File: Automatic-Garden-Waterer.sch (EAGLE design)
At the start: 14 parts, among them K1 AQG12105, X1 6ESRM-P

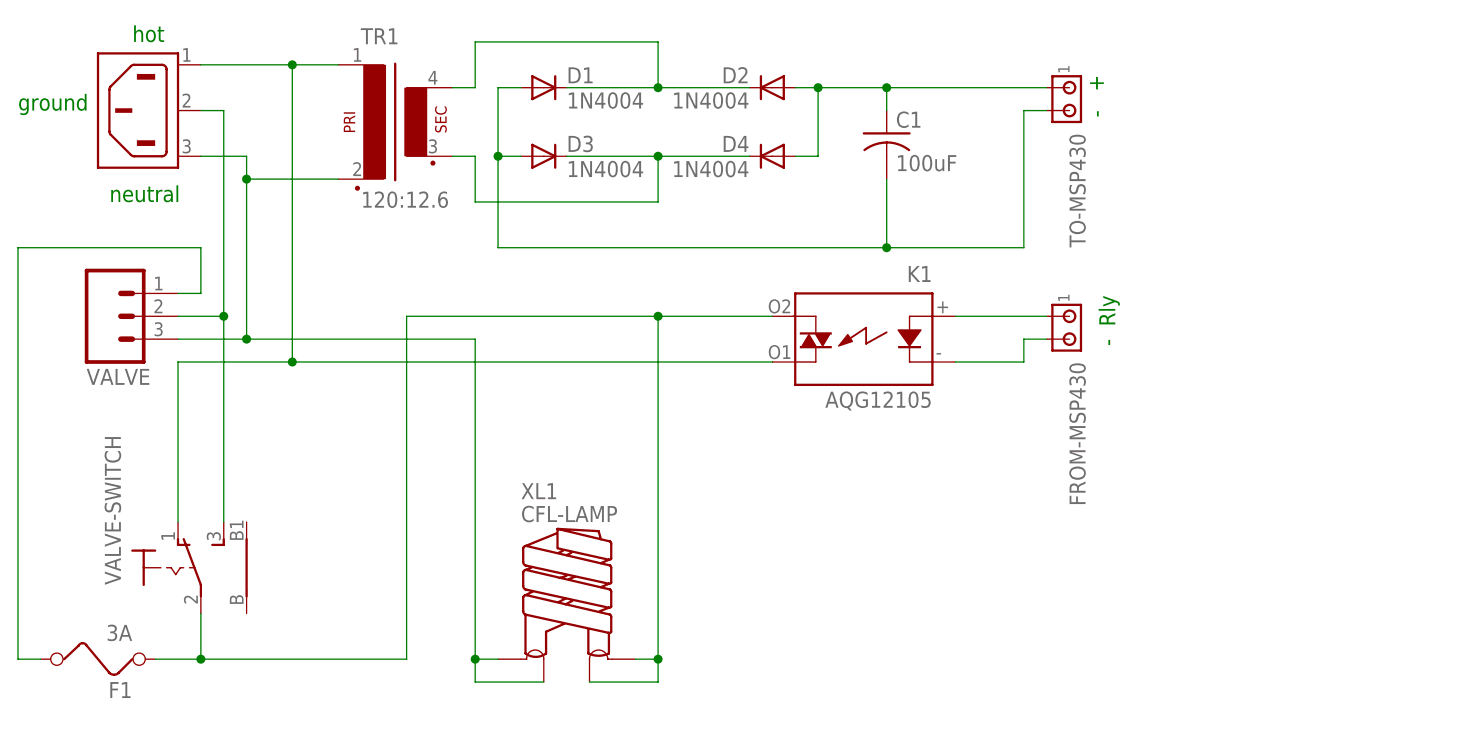
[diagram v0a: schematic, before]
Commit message: modified because valve is normally open
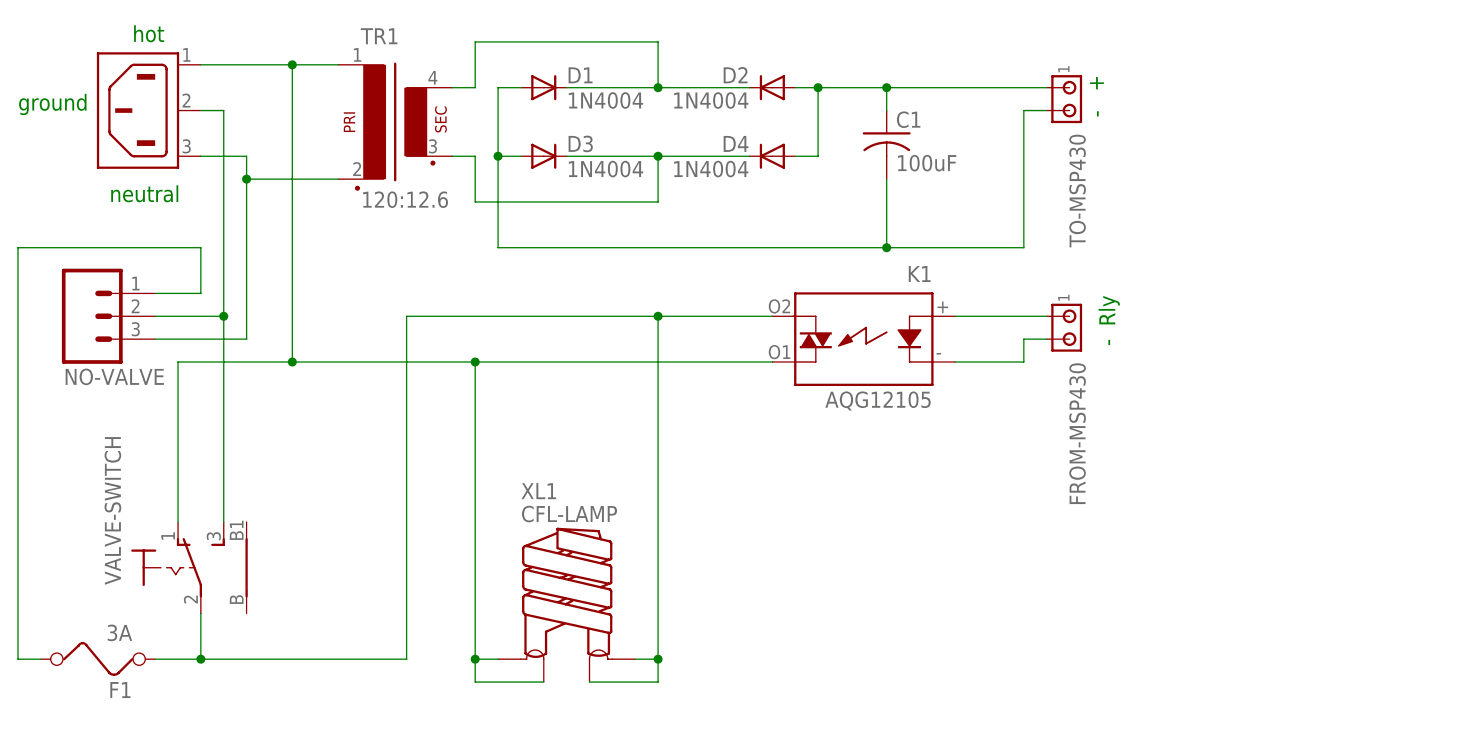
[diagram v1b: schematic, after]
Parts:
- removed VALVE: (no value), SparkFun:M03PTH
- added NO-VALVE: (no value), SparkFun:M03PTH
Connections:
- removed net N$5: K1.DS2, TR1.P1, VALVE-SWITCH.O, X1.AC1
- new net N$2: NO-VALVE.3, TR1.P2, X1.AC2
- net N$10: now also NO-VALVE.2; no longer VALVE.2
- net N$13: now also NO-VALVE.1; no longer VALVE.1
- net N$6: now also K1.DS2, TR1.P1, VALVE-SWITCH.O, X1.AC1; no longer TR1.P2, VALVE.3, X1.AC2
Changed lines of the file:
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@@
 <part name="X1" library="con-tycoelectronics" deviceset="6ESRM-P" device=""/>
 <part name="XL1" library="ir" deviceset="CFL-LAMP" device=""/>
-<part name="VALVE" library="SparkFun" deviceset="M03" device="PTH"/>
+<part name="NO-VALVE" library="SparkFun" deviceset="M03" device="PTH"/>
 <part name="VALVE-SWITCH" library="switch" deviceset="316-917" device=""/>
 </parts>
@@
 <instance part="X1" gate="G$1" x="-15.24" y="53.34" rot="MR0"/>
 <instance part="XL1" gate="G$1" x="27.94" y="-2.54"/>
-<instance part="VALVE" gate="G$1" x="-22.86" y="30.48" rot="MR180"/>
+<instance part="NO-VALVE" gate="G$1" x="-25.4" y="30.48" rot="MR180"/>
 <instance part="VALVE-SWITCH" gate="1" x="-15.24" y="2.54"/>
 </instances>
@@
 <net name="N$6" class="0">
 <segment>
-<pinref part="X1" gate="G$1" pin="AC2"/>
-<wire x1="-12.7" y1="48.26" x2="-7.62" y2="48.26" width="0.1524" layer="91"/>
-<wire x1="-7.62" y1="48.26" x2="-7.62" y2="45.72" width="0.1524" layer="91"/>
-<pinref part="TR1" gate="1" pin="P2"/>
-<wire x1="-7.62" y1="45.72" x2="2.54" y2="45.72" width="0.1524" layer="91"/>
-<pinref part="VALVE" gate="G$1" pin="3"/>
-<wire x1="-15.24" y1="27.94" x2="-7.62" y2="27.94" width="0.1524" layer="91"/>
-<wire x1="-7.62" y1="27.94" x2="-7.62" y2="45.72" width="0.1524" layer="91"/>
-<junction x="-7.62" y="45.72"/>
 <pinref part="XL1" gate="G$1" pin="1"/>
 <wire x1="20.32" y1="-7.62" x2="17.78" y2="-7.62" width="0.1524" layer="91"/>
@@
 <wire x1="17.78" y1="-10.16" x2="17.78" y2="-7.62" width="0.1524" layer="91"/>
 <junction x="17.78" y="-7.62"/>
-<wire x1="-7.62" y1="27.94" x2="17.78" y2="27.94" width="0.1524" layer="91"/>
-<wire x1="17.78" y1="27.94" x2="17.78" y2="-7.62" width="0.1524" layer="91"/>
-<junction x="-7.62" y="27.94"/>
-</segment>
-</net>
-<net name="N$5" class="0">
-<segment>
 <pinref part="TR1" gate="1" pin="P1"/>
 <pinref part="X1" gate="G$1" pin="AC1"/>
@@
 <wire x1="-2.54" y1="58.42" x2="-2.54" y2="25.4" width="0.1524" layer="91"/>
 <pinref part="K1" gate="A" pin="DS2"/>
-<wire x1="50.8" y1="25.4" x2="-2.54" y2="25.4" width="0.1524" layer="91"/>
+<wire x1="50.8" y1="25.4" x2="17.78" y2="25.4" width="0.1524" layer="91"/>
 <pinref part="VALVE-SWITCH" gate="1" pin="O"/>
+<wire x1="17.78" y1="25.4" x2="-2.54" y2="25.4" width="0.1524" layer="91"/>
 <wire x1="-15.24" y1="7.62" x2="-15.24" y2="25.4" width="0.1524" layer="91"/>
 <wire x1="-15.24" y1="25.4" x2="-2.54" y2="25.4" width="0.1524" layer="91"/>
 <junction x="-2.54" y="25.4"/>
+<wire x1="17.78" y1="-7.62" x2="17.78" y2="25.4" width="0.1524" layer="91"/>
+<junction x="17.78" y="25.4"/>
 </segment>
 </net>
@@
 <wire x1="-12.7" y1="53.34" x2="-10.16" y2="53.34" width="0.1524" layer="91"/>
 <wire x1="-10.16" y1="53.34" x2="-10.16" y2="30.48" width="0.1524" layer="91"/>
-<pinref part="VALVE" gate="G$1" pin="2"/>
-<wire x1="-10.16" y1="30.48" x2="-15.24" y2="30.48" width="0.1524" layer="91"/>
+<pinref part="NO-VALVE" gate="G$1" pin="2"/>
+<wire x1="-10.16" y1="30.48" x2="-17.78" y2="30.48" width="0.1524" layer="91"/>
 <junction x="-10.16" y="30.48"/>
 <pinref part="VALVE-SWITCH" gate="1" pin="S"/>
@@
 <wire x1="-33.02" y1="38.1" x2="-12.7" y2="38.1" width="0.1524" layer="91"/>
 <wire x1="-12.7" y1="38.1" x2="-12.7" y2="33.02" width="0.1524" layer="91"/>
-<pinref part="VALVE" gate="G$1" pin="1"/>
-<wire x1="-12.7" y1="33.02" x2="-15.24" y2="33.02" width="0.1524" layer="91"/>
+<pinref part="NO-VALVE" gate="G$1" pin="1"/>
+<wire x1="-12.7" y1="33.02" x2="-17.78" y2="33.02" width="0.1524" layer="91"/>
 </segment>
 </net>
+<net name="N$2" class="0">
+<segment>
+<pinref part="TR1" gate="1" pin="P2"/>
+<pinref part="X1" gate="G$1" pin="AC2"/>
+<wire x1="-12.7" y1="48.26" x2="-7.62" y2="48.26" width="0.1524" layer="91"/>
+<wire x1="-7.62" y1="48.26" x2="-7.62" y2="45.72" width="0.1524" layer="91"/>
+<wire x1="-7.62" y1="45.72" x2="2.54" y2="45.72" width="0.1524" layer="91"/>
+<junction x="-7.62" y="45.72"/>
+<wire x1="-7.62" y1="27.94" x2="-7.62" y2="45.72" width="0.1524" layer="91"/>
+<pinref part="NO-VALVE" gate="G$1" pin="3"/>
+<wire x1="-17.78" y1="27.94" x2="-7.62" y2="27.94" width="0.1524" layer="91"/>
+</segment>
+</net>

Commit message: changed to final schematics
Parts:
- removed FROM-MSP430, TO-MSP430: (no value), con-amp:MTA02-100
- removed VALVE-SWITCH: (no value), switch:316-917
- removed XL1: CFL-LAMP, ir:CFL-LAMP
- added C2: 0.33uF, rcl:C-US075-032X103
- added C3: 1uF, rcl:C-US075-032X103
- added D5: HLMP6, display-hp:HLMP6
- added IC1: (no value), SparkFun:V_REG_78XXSIDE
- added POWER-TO_ARDUINO: (no value), con-amp:MTA02-100
- added SOLENOID-FROM_ARDUINO: 350760-4, con-amp:350760-4
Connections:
- new net N$15: C1.2, C2.2, C3.2, D1.A, D3.A, IC1.GND, POWER-TO_ARDUINO.2
- new net N$5: D5.K, SOLENOID-FROM_ARDUINO.3
- net N$1: now also C3.1, IC1.OUT, POWER-TO_ARDUINO.1; no longer C1.2, D1.A, D3.A, TO-MSP430.2
- net N$10: no longer VALVE-SWITCH.S
- net N$12: no longer VALVE-SWITCH.P, XL1.2, XL1.4
- net N$6: no longer VALVE-SWITCH.O, XL1.1, XL1.3
- net N$7: now also SOLENOID-FROM_ARDUINO.1; no longer FROM-MSP430.1
- net N$8: now also D5.A, SOLENOID-FROM_ARDUINO.2; no longer FROM-MSP430.2
- net N$9: now also C2.1, IC1.IN; no longer TO-MSP430.1
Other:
- note added: "LED - Rly"
- note removed: "- Rly"
- moved on the sheet: C1
